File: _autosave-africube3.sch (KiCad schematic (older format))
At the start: 30 parts, among them J1 SMA Edge FM, J2 Conn_01x04, J3 RPi_GPIO, J4 Conn_01x02, U1 TQP7M9105, U2 SXBP-150+, U3 BA178M05FP-E2

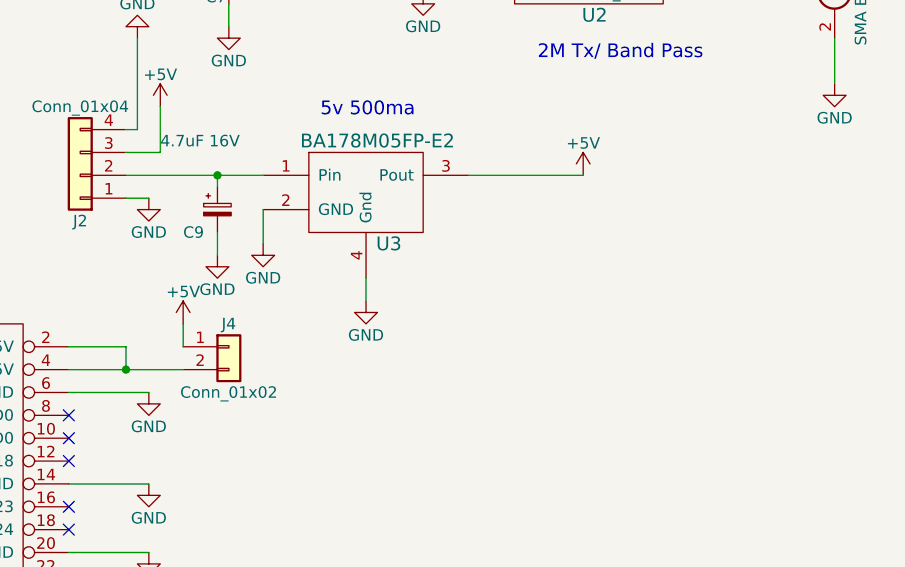
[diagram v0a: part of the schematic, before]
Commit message: updated the pcd file to africube 4 by readding inductor L5
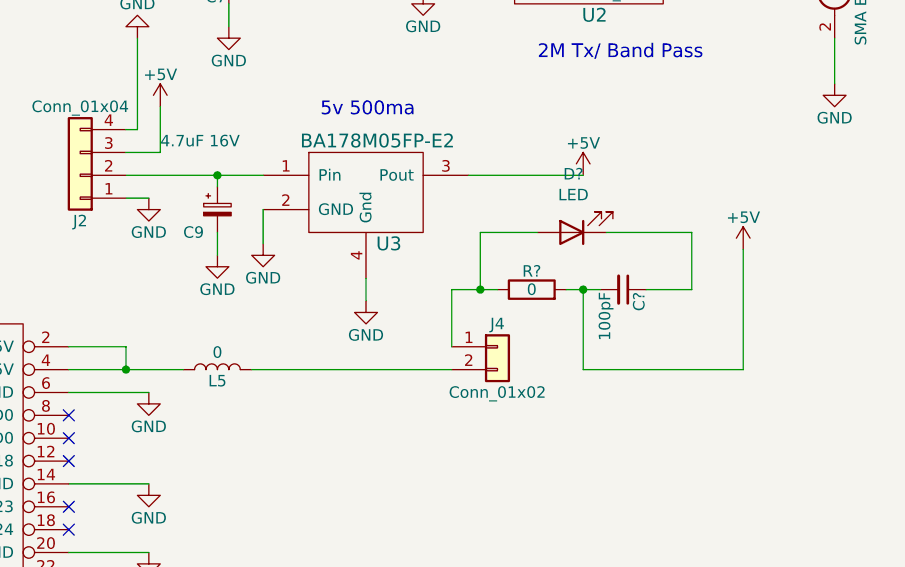
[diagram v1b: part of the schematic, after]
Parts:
- added C?: 100pF, Capacitors_SMD:C_0805_HandSoldering, symbol africube3-rescue:C_Small-_saved_africube2-cache
- added D?: LED, symbol Device:LED
- added L5: 0, Resistors_SMD:R_0805_HandSoldering, symbol africube3-rescue:L-_saved_africube2-cache
- added R?: 0, Resistors_SMD:R_0805_HandSoldering, symbol africube3-rescue:R-_saved_africube2-cache
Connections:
- wire segments 90 -> 103
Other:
- moved on the sheet: J4
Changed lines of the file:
@@
-$EndComp
-$Comp
-L power:+5V #PWR012
-U 1 1 5D28CE0E
-P 5400 3650
-F 0 "#PWR012" H 5400 3500 50  0001 C CNN
-F 1 "+5V" H 5400 3790 50  0000 C CNN
-F 2 "" H 5400 3650 50  0001 C CNN
-F 3 "" H 5400 3650 50  0001 C CNN
-	1    5400 3650
-	1    0    0    -1
 $EndComp
 $Comp
@@
 L africube3-rescue:Conn_01x02-_saved_africube2-cache J4
 U 1 1 5D319F18
-P 5600 3750
-F 0 "J4" H 5600 3850 50  0000 C CNN
-F 1 "Conn_01x02" H 5600 3550 50  0000 C CNN
-F 2 "Pin_Headers:Pin_Header_Straight_1x02_Pitch2.54mm" H 5600 3750 50  0001 C CNN
-F 3 "" H 5600 3750 50  0001 C CNN
-	1    5600 3750
+P 6775 3750
+F 0 "J4" H 6775 3850 50  0000 C CNN
+F 1 "Conn_01x02" H 6775 3550 50  0000 C CNN
+F 2 "Pin_Headers:Pin_Header_Straight_1x02_Pitch2.54mm" H 6775 3750 50  0001 C CNN
+F 3 "" H 6775 3750 50  0001 C CNN
+	1    6775 3750
 	1    0    0    -1
 $EndComp
@@
 Wire Wire Line
 	4900 3850 5150 3850
-Wire Wire Line
-	5400 3650 5400 3750
 Wire Wire Line
 	6450 2000 6450 2100
@@
 	1    0    0    -1
 $EndComp
+$Comp
+L africube3-rescue:L-_saved_africube2-cache L5
+U 1 1 61F2B5FB
+P 5550 3850
+F 0 "L5" V 5500 3850 50  0000 C CNN
+F 1 "0" V 5625 3850 50  0000 C CNN
+F 2 "Resistors_SMD:R_0805_HandSoldering" H 5550 3850 50  0001 C CNN
+F 3 "" H 5550 3850 50  0001 C CNN
+	1    5550 3850
+	0    -1   -1   0
+$EndComp
+Wire Wire Line
+	5700 3850 6575 3850
+$Comp
+L power:+5V #PWR012
+U 1 1 5D28CE0E
+P 7850 3325
+F 0 "#PWR012" H 7850 3175 50  0001 C CNN
+F 1 "+5V" H 7850 3465 50  0000 C CNN
+F 2 "" H 7850 3325 50  0001 C CNN
+F 3 "" H 7850 3325 50  0001 C CNN
+	1    7850 3325
+	1    0    0    -1
+$EndComp
+Wire Wire Line
+	6575 3750 6575 3500
+Wire Wire Line
+	6575 3500 6700 3500
+$Comp
+L africube3-rescue:R-_saved_africube2-cache R?
+U 1 1 61F3E0D6
+P 6925 3500
+F 0 "R?" V 7005 3500 50  0000 C CNN
+F 1 "0" V 6925 3500 50  0000 C CNN
+F 2 "Resistors_SMD:R_0805_HandSoldering" V 6855 3500 50  0001 C CNN
+F 3 "" H 6925 3500 50  0001 C CNN
+	1    6925 3500
+	0    -1   -1   0
+$EndComp
+$Comp
+L africube3-rescue:C_Small-_saved_africube2-cache C?
+U 1 1 61F3F58B
+P 7325 3500
+F 0 "C?" H 7335 3570 50  0000 L CNN
+F 1 "100pF" H 7335 3420 50  0000 L CNN
+F 2 "Capacitors_SMD:C_0805_HandSoldering" H 7325 3500 50  0001 C CNN
+F 3 "" H 7325 3500 50  0001 C CNN
+	1    7325 3500
+	0    1    1    0
+$EndComp
+$Comp
+L Device:LED D?
+U 1 1 61F405DB
+P 7100 3250
+F 0 "D?" H 7093 2995 50  0000 C CNN
+F 1 "LED" H 7093 3086 50  0000 C CNN
+F 2 "" H 7100 3250 50  0001 C CNN
+F 3 "~" H 7100 3250 50  0001 C CNN
+	1    7100 3250
+	-1   0    0    1
+$EndComp
+Wire Wire Line
+	6700 3500 6700 3250
+Wire Wire Line
+	6700 3250 6950 3250
+Connection ~ 6700 3500
+Wire Wire Line
+	6700 3500 6775 3500
+Wire Wire Line
+	7250 3250 7625 3250
+Wire Wire Line
+	7625 3250 7625 3500
+Wire Wire Line
+	7625 3500 7425 3500
+Wire Wire Line
+	7075 3500 7150 3500
+Wire Wire Line
+	7150 3500 7150 3850
+Wire Wire Line
+	7150 3850 7850 3850
+Wire Wire Line
+	7850 3325 7850 3850
+Connection ~ 7150 3500
+Wire Wire Line
+	7150 3500 7225 3500
 $EndSCHEMATC
